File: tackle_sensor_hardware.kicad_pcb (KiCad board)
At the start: 2 copper layers, 50.8 x 50.8 mm, 77 parts, among them J1 Conn_01x02_Male, J2 Conn_01x04_Male, J3 Conn_01x03_Male, J4 Conn_ARM_JTAG_SWD_10, Q1 DMP4051LK3, Q2 2N7002K, Q3 2N7002K, Q4 2N7002K, Q5 2N7002K, Q6 2N7002K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

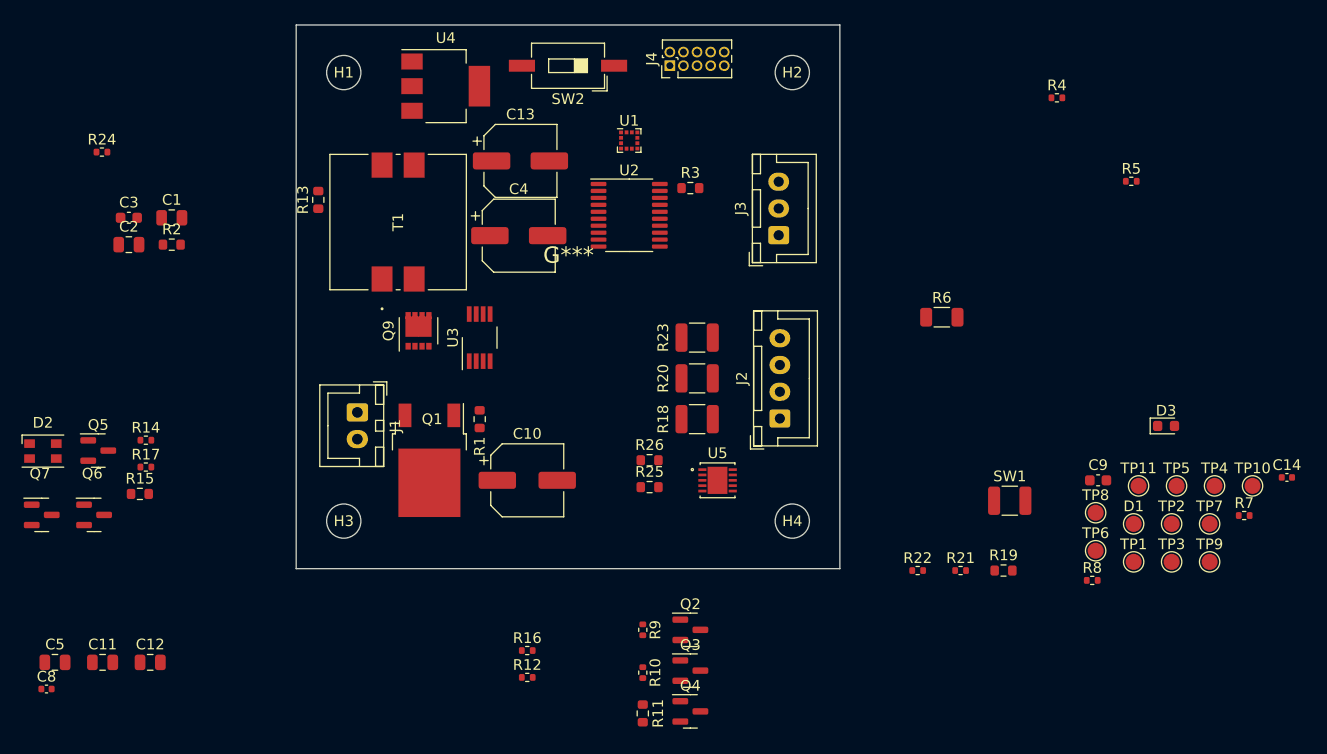
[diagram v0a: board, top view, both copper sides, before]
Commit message: updated component placement and board size, cleaning up schamtic and part selection.
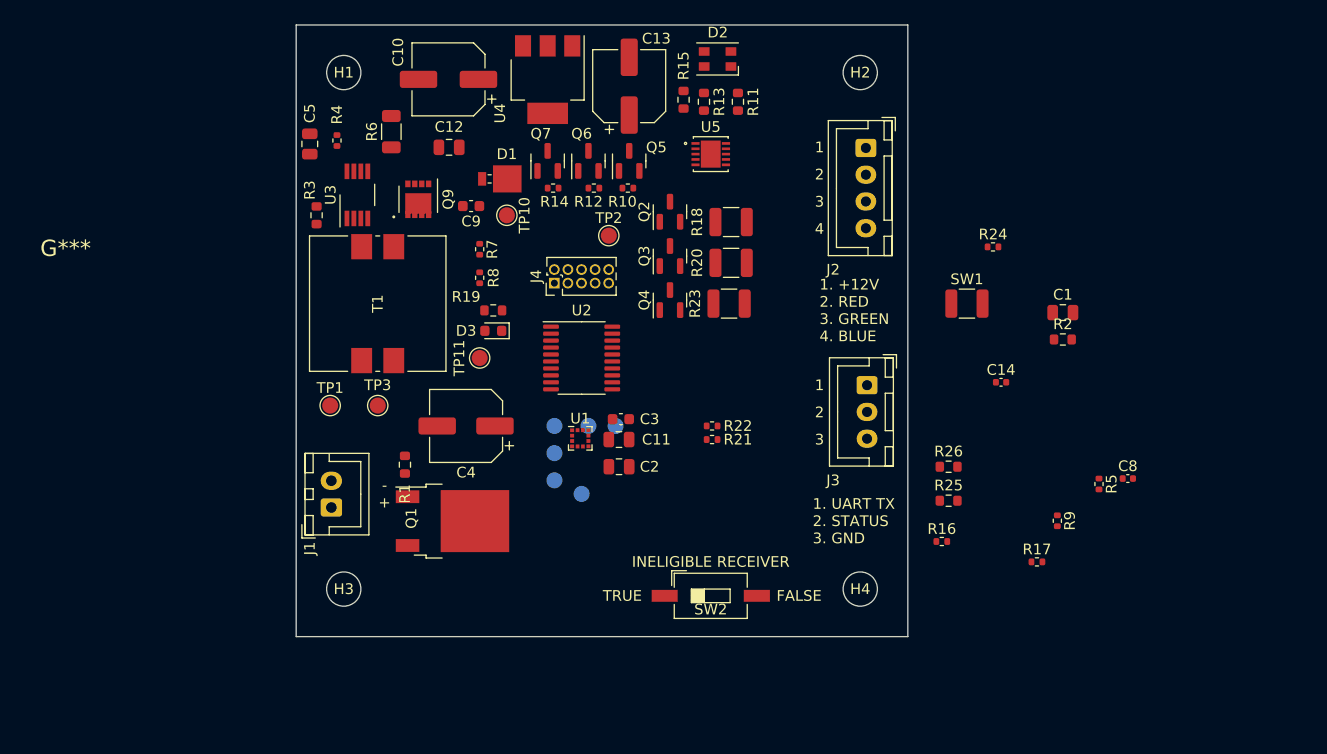
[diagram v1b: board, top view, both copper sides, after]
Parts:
- D1: footprint TestPoint:TestPoint_Pad_D1.5mm -> Diode_SMD:D_Powermite_AK
- TP4, TP5, TP6, TP7, TP8, TP9: moved to B.Cu
- moved C8 102.9 mm to (198.4, 112.2)
- moved R17 83.7 mm to (189.9, 120.0)
- moved C1 83.7 mm to (192.3, 96.7)
- moved R2 83.7 mm to (192.3, 99.2)
- moved R24 83.7 mm to (185.8, 90.6)
- moved TP1 76.5 mm to (123.8, 105.4)
- moved R7 75.6 mm to (137.8, 90.8), turned to -90 degrees
- moved TP3 75.6 mm to (128.3, 105.4)
- moved TP10 74.1 mm to (140.3, 87.6), turned to -90 degrees
- moved D2 72.9 mm to (160.0, 73.0), turned to 180 degrees
- moved D1 67.4 mm to (139.7, 84.2), turned to 180 degrees
- moved R4 67.4 mm to (124.5, 80.6), turned to 90 degrees
- moved C9 63.9 mm to (137.0, 86.8), turned to 180 degrees
- moved R8 63.8 mm to (137.8, 93.5), turned to -90 degrees
- moved D3 63.5 mm to (139.1, 98.4), turned to 180 degrees
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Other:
- board size 50.8 x 50.8 mm -> 57.2 x 57.2 mm
- board text added: "- +"
- board text added: "1"
- board text added: "1. +12V 2. RED 3. GREEN 4. BLUE"
- board text added: "1. UART TX 2. STATUS 3. GND"
- board text added: "2"
- board text added: "3"
- board text added: "4"
- board text added: "FALSE"
- board text added: "INELIGIBLE RECEIVER"
- board text added: "TRUE"

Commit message: routing in progress.
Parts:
- added C6: C, Capacitor_SMD:C_0402_1005Metric, F.Cu at (113.8, 88.1)
- added C7: C, Capacitor_SMD:C_0402_1005Metric, F.Cu at (110.9, 88.1)
- added D4: BZT52-B15_R1_00001, Diode_SMD:D_SOD-123, F.Cu at (132.3, 113.9)
- added TP12: TestPoint, TestPoint:TestPoint_Pad_D1.5mm, F.Cu at (153.7, 99.9)
- added TP13: TestPoint, TestPoint:TestPoint_Pad_D1.5mm, B.Cu at (147.1, 103.9)
- added TP14: TestPoint, TestPoint:TestPoint_Pad_D1.5mm, B.Cu at (141.2, 103.9)
- R1: value 1k,1%,25mW -> 10k,1%,63mW; footprint Resistor_SMD:R_0603_1608Metric -> Resistor_SMD:R_0402_1005Metric
- R18, R20, R23: value 0 -> 0,0.5W
- R2: value 0 -> 0,63mW; footprint Resistor_SMD:R_0603_1608Metric -> Resistor_SMD:R_0402_1005Metric
- R3: footprint Resistor_SMD:R_0603_1608Metric -> Resistor_SMD:R_0402_1005Metric
- moved R17 41.7 mm to (161.5, 89.4)
- moved R16 39.2 mm to (161.5, 84.1)
- moved R24 25.1 mm to (161.0, 95.0)
- moved U3 14.5 mm to (112.4, 81.9)
- moved U5 9.74 mm to (166.9, 75.7)
- moved R22 8.98 mm to (167.6, 103.5)
- moved R21 8.87 mm to (167.6, 105.0)
- moved C9 8.87 mm to (128.1, 87.0)
- moved Q2 8.11 mm to (161.1, 81.4)
- moved R23 7.99 mm to (166.7, 90.2)
- moved R20 7.68 mm to (166.7, 86.6)
- moved D1 7.55 mm to (132.7, 87.0)
- moved R18 7.50 mm to (166.7, 83.1)
- moved Q3 7.34 mm to (161.1, 86.6)
- moved Q4 6.42 mm to (161.1, 92.3)
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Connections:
- U2 pad 17: unconnected-(U2-Pad17) -> Net-(TP12-Pad1)
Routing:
- net GND: track 0.00 -> 39.3 mm, vias 0 -> 16
- net Net-(C4-Pad1): track 0.00 -> 20.4 mm
- net +3V3: track 0.00 -> 12.7 mm, vias 0 -> 3
- net Net-(J1-Pad1): track 0.00 -> 12.4 mm
- net Net-(D4-Pad2): track 0.00 -> 6.62 mm
- net Net-(J2-Pad4): track 0.00 -> 6.28 mm
- net Net-(J2-Pad2): track 0.00 -> 6.06 mm
- net +12V: track 0.00 -> 5.88 mm
- net Net-(J2-Pad3): track 0.00 -> 5.85 mm
- net Net-(C9-Pad2): track 0.00 -> 5.80 mm
- net Net-(Q2-Pad3): track 0.00 -> 5.72 mm
- net Net-(Q4-Pad3): track 0.00 -> 4.61 mm
- net Net-(Q3-Pad3): track 0.00 -> 4.51 mm
- net G_PWM: track 0.00 -> 2.37 mm
- net R_PWM: track 0.00 -> 2.14 mm
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- added copper zone on F.Cu, net +12V
- added copper zone on In2.Cu, net +3V3
- added copper zone on F.Cu, net GND
- added copper zone on In1.Cu, net GND
- added copper zone on F.Cu, net Net-(C9-Pad1)
- added copper zone on F.Cu, net Net-(C9-Pad2)
- added copper zone on F.Cu, net Net-(Q9-Pad1)
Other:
- copper layers 2 -> 4

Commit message: update reset button, add decoupling caps for MCU.
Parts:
- added C15: 100nF, 50V, Capacitor_SMD:C_0805_2012Metric, F.Cu at (192.7, 104.4)
- added C16: 1uF, 50V, Capacitor_SMD:C_0603_1608Metric, F.Cu at (196.9, 104.1)
- SW1: value SW_Push -> PTS645SL43SMTR92 LFS; footprint Resistor_SMD:R_1210_3225Metric -> Button_Switch_SMD:SW_SPST_PTS645
- moved C1 37.9 mm to (154.4, 96.8), turned to 90 degrees
- moved SW1 35.6 mm to (147.8, 98.3), turned to 180 degrees
- moved C11 6.86 mm to (150.9, 115.4)
- moved C2 6.86 mm to (150.9, 118.0)
- moved TP12 6.86 mm to (153.8, 106.8)
- moved TP13 6.86 mm to (147.2, 110.7)
- moved TP14 6.86 mm to (141.4, 110.7)
- moved TP6 6.86 mm to (144.9, 119.3)
- moved TP7 6.86 mm to (144.9, 114.2)
- moved TP9 6.86 mm to (150.6, 114.2)
- moved U1 6.86 mm to (147.3, 115.3)
- moved TP8 6.86 mm to (148.1, 114.2)
- moved TP4 6.86 mm to (144.9, 116.7)
- moved TP5 6.86 mm to (147.4, 120.5)
- moved U2 6.86 mm to (147.4, 107.8)
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
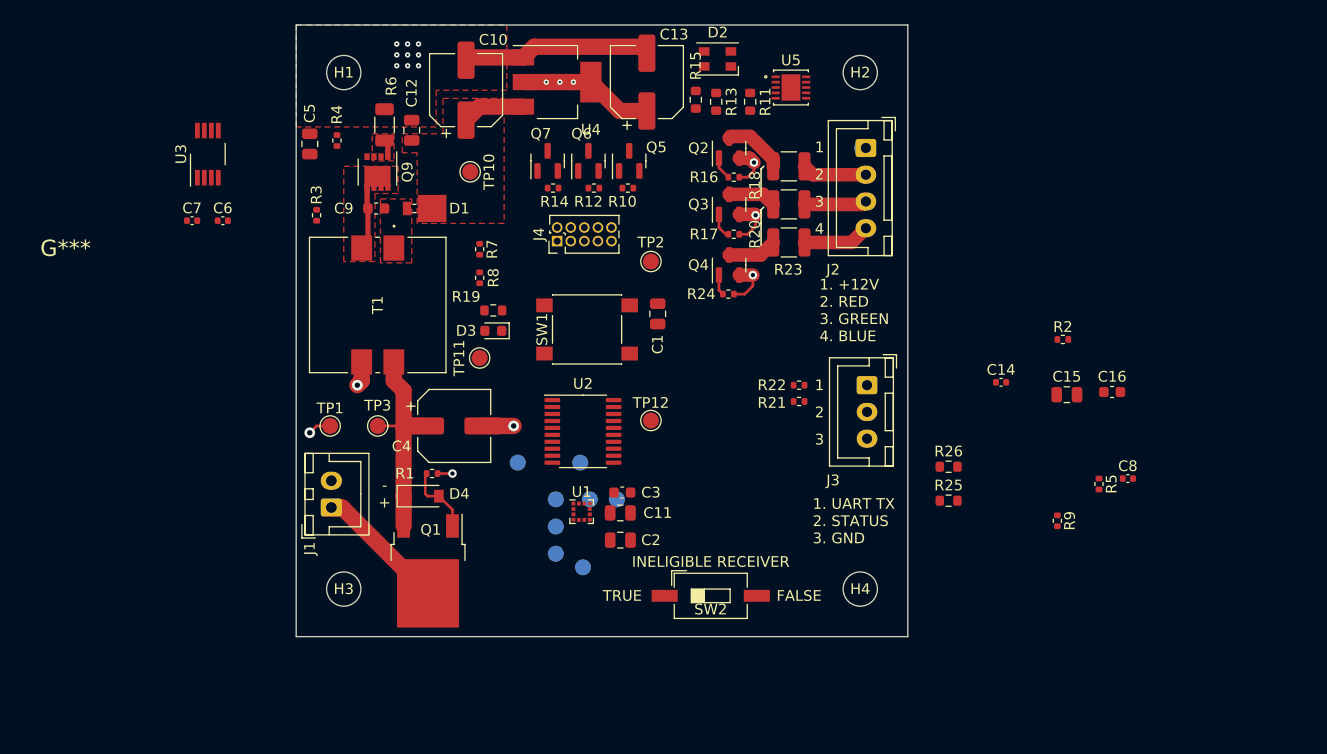
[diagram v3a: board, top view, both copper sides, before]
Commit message: added PTC
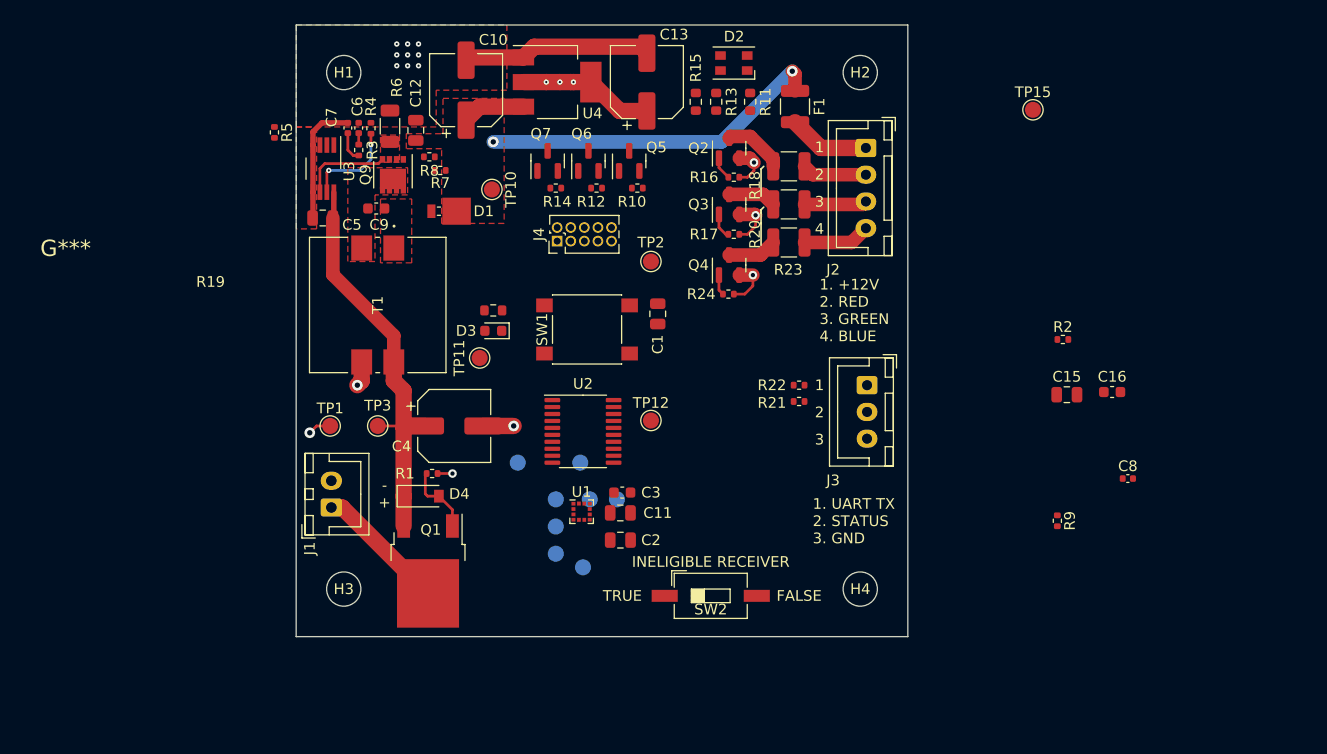
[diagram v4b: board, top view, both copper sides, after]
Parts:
- removed C14: DNP, Capacitor_SMD:C_0402_1005Metric
- removed R25, R26: 1k, Resistor_SMD:R_0603_1608Metric
- removed U5: NIS5420MT6TXG, rfc_footprint_lib:WDFN10_522AA-01_ONS
- added F1: MF-USHT035KX-2, Resistor_SMD:R_1210_3225Metric, F.Cu at (167.3, 77.5)
- added TP15: TestPoint, TestPoint:TestPoint_Pad_D1.5mm, F.Cu at (189.5, 77.8)
- moved R5 83.8 mm to (118.6, 79.9)
- moved C7 16.9 mm to (125.5, 79.5), turned to 90 degrees
- moved C6 15.4 mm to (126.5, 79.5), turned to 90 degrees
- moved R8 12.2 mm to (133.1, 82.2), turned to 180 degrees
- moved U3 10.9 mm to (123.2, 83.3), turned to -90 degrees
- moved R7 8.24 mm to (134.1, 83.4), turned to 180 degrees
- moved R3 7.26 mm to (126.5, 81.5)
- moved C5 7.02 mm to (123.1, 87.9), turned to 180 degrees
- moved R4 3.38 mm to (127.6, 79.5)
- moved TP10 2.62 mm to (138.9, 85.2)
- moved D1 2.30 mm to (134.9, 87.2)
- moved D2 1.57 mm to (161.5, 73.4)
- moved Q9 1.47 mm to (129.7, 83.8)
- moved R10 0.89 mm to (152.5, 85.1)
- moved R6 0.52 mm to (129.4, 79.3)
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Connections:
- U2 pad 1: EN_FAULT_EFUSE -> Net-(U2-Pad1)
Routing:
- net +12V: track 5.88 -> 38.5 mm, vias 0 -> 2
- net Net-(C4-Pad1): track 20.4 -> 38.6 mm
- net GND: track 39.3 -> 51.0 mm
- net Net-(R4-Pad1): track 0.00 -> 8.88 mm, vias 0 -> 2
- net Net-(Q9-Pad4): track 0.00 -> 8.42 mm
- net Net-(J2-Pad1): track 0.34 -> 7.62 mm
- net Net-(C9-Pad2): track 5.80 -> 0.94 mm
- net Net-(C7-Pad1): track 0.00 -> 2.81 mm
- net Net-(Q9-Pad1): track 1.64 -> 0.44 mm
- net Net-(C6-Pad1): track 0.00 -> 1.07 mm

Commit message: route board
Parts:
- moved C8 77.8 mm to (126.1, 83.3)
- moved C16 51.9 mm to (145.3, 109.9), turned to 180 degrees
- moved TP15 50.5 mm to (146.4, 104.1)
- moved R9 49.9 mm to (141.9, 118.1), turned to 0 degrees
- moved C15 47.4 mm to (145.3, 108.0), turned to 180 degrees
- moved R2 46.5 mm to (149.4, 117.1), turned to -90 degrees
- moved TP6 20.1 mm to (162.6, 109.7)
- moved TP5 17.8 mm to (159.3, 107.2)
- moved TP4 16.9 mm to (161.5, 113.9), turned to -90 degrees
- moved TP14 14.3 mm to (154.4, 105.0)
- moved SW2 12.7 mm to (146.7, 123.1)
- moved TP9 9.06 mm to (159.4, 111.9)
- moved C3 8.53 mm to (157.1, 119.6)
- moved R5 7.83 mm to (126.1, 82.2), turned to 0 degrees
- moved TP12 7.44 mm to (160.4, 103.4)
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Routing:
- net B_PWM: track 1.93 -> 42.3 mm
- net G_PWM: track 2.37 -> 41.5 mm, vias 0 -> 2
- net /RST: track 0.00 -> 35.3 mm
- net GND: track 51.0 -> 85.5 mm, vias 16 -> 33
- net R_PWM: track 2.14 -> 36.2 mm, vias 0 -> 2
- net /SWDIO: track 0.00 -> 31.6 mm
- net /SWCLK: track 0.00 -> 28.3 mm
- net UART_TX: track 0.00 -> 28.2 mm, vias 0 -> 2
- net +3V3: track 12.7 -> 34.2 mm, vias 3 -> 9
- net TACKLE_STATUS: track 0.00 -> 20.7 mm, vias 0 -> 2
- net Net-(R9-Pad2): track 0.00 -> 20.3 mm, vias 0 -> 2
- net Net-(R7-Pad2): track 0.00 -> 19.0 mm, vias 0 -> 2
- net /ACC_INT1: track 0.00 -> 16.8 mm, vias 0 -> 3
- net /SPI1_MISO: track 0.00 -> 15.4 mm, vias 0 -> 1
- net Net-(Q7-Pad3): track 0.00 -> 15.0 mm
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- added copper zone on F.Cu, net +3V3
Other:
- board text added: "Robotic Football Tackle Sensor V0.0 4/18/2022"
- board text removed: "Robotic Football Tackle Sensor V0.0 4/15/2022"

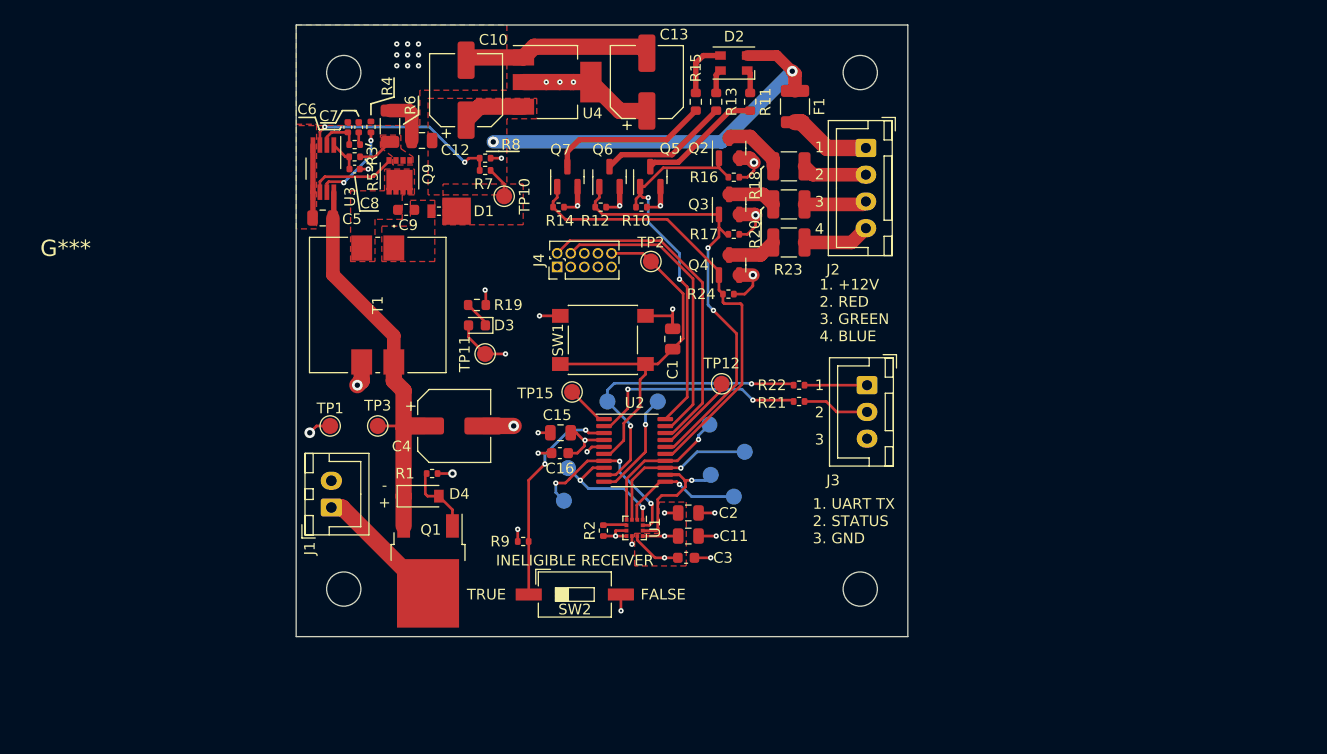
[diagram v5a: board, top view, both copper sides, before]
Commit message: finish route, add release pacakage
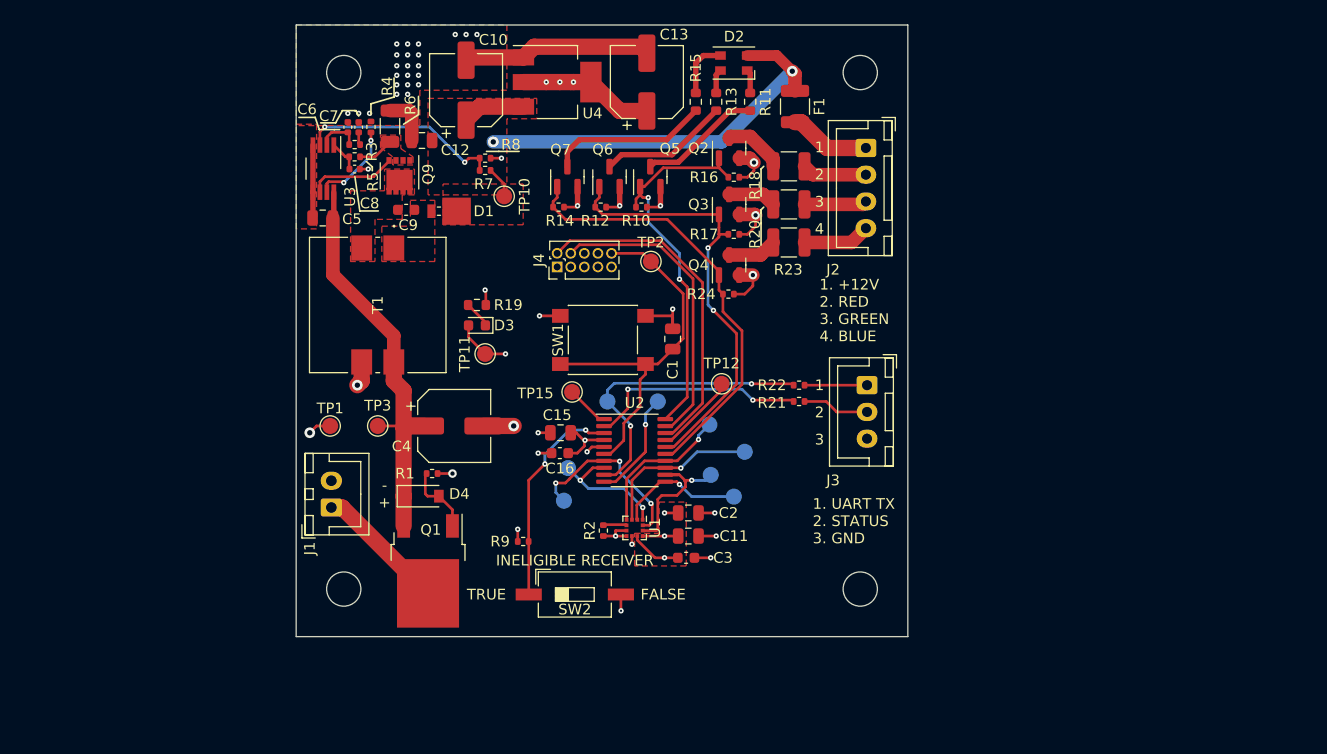
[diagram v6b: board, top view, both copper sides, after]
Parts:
- C6: value C -> 2200pF,10%,50V
- C7: value C -> 0.22uF,10%,35V
- R3: value R_US -> 634,.1%,0.1W
- moved G*** 48.8 mm to (147.1, 81.8)
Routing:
- net B_PWM: track 42.3 -> 41.4 mm
- net GND: vias 33 -> 47
